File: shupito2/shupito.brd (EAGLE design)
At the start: 41.9 x 26 mm, 84 parts, among them IC2 74LVC1T45, IC3 74LVC1T45, IC4 74LVC1T45, IC5 74LVC1T45, IC6 ATXMEGA32A4U-AU, IC7 TPS73033DBV, Q1 BC807W-1907646, Q10 1758094, Q11 PDTC123YU-1757992, Q2 NX2301P-1894738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

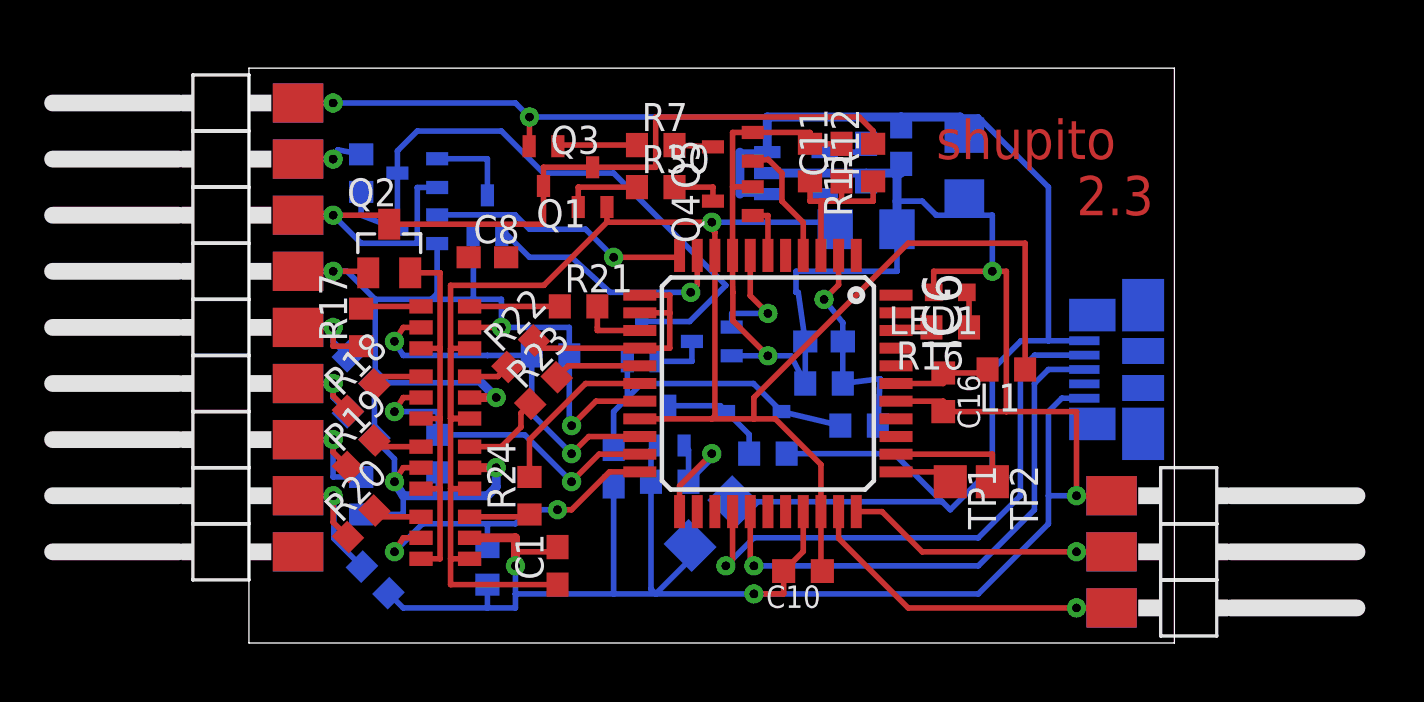
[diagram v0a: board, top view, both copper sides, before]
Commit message: Added a button, placement and routing.
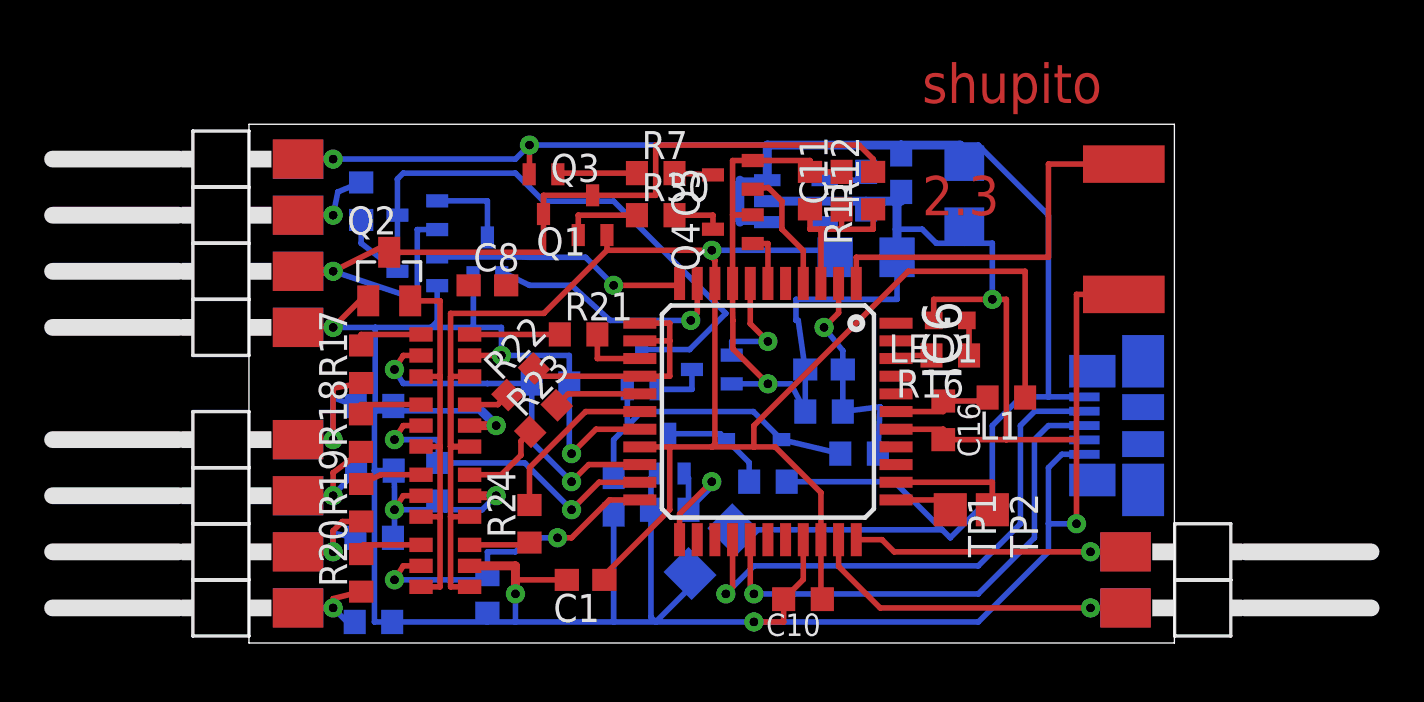
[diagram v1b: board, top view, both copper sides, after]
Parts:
- removed JP19, JP20, JP25, JP27: PINH1X01SMD, pinhead_smd:PINH1X01SMD
- added S1: KSS241G, switch:KSS-G
- moved JP1 5.08 mm to (0.00, 9.53)
- moved JP12 5.08 mm to (0.00, 9.53)
- moved JP15 5.08 mm to (0.00, 4.45)
- moved JP16 5.08 mm to (0.00, 1.91)
- moved JP3 5.08 mm to (0.00, 4.45)
- moved JP4 5.08 mm to (0.00, 1.91)
- moved JP14 5.08 mm to (0.00, 6.99)
- moved JP2 5.08 mm to (0.00, 6.99)
- moved JP23 2.54 mm to (0.00, 19.7)
- moved JP24 2.54 mm to (0.00, 19.7)
- moved JP11 2.54 mm to (0.00, 22.2)
- moved JP13 2.54 mm to (0.00, 17.1)
- moved JP17 2.54 mm to (0.00, 14.6)
- moved JP18 2.54 mm to (0.00, 22.2)
- moved JP5 2.54 mm to (0.00, 17.1)
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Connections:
- new net BTN: IC6.1, S1.2
- net GND: now also S1.1; no longer JP19.1, JP20.1
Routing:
- net BTN: track 0.00 -> 17.5 mm
- net GND: track 205.0 -> 213.4 mm
- net N$37: track 9.09 -> 6.14 mm
- net N$35: track 6.88 -> 9.79 mm
- net D-: track 26.1 -> 24.8 mm
- net D+: track 24.5 -> 23.2 mm
- net VCC: track 92.5 -> 93.7 mm
- net N$7: track 6.27 -> 7.33 mm
- net N$9: track 2.25 -> 3.16 mm
- net N$27: track 2.23 -> 3.04 mm
- net N$8: track 4.72 -> 5.39 mm
- net VCCIO: track 41.5 -> 42.1 mm
- net N$25: track 2.23 -> 2.80 mm
- net N$36: track 7.97 -> 7.45 mm
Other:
- board size 41.9 x 26 mm -> 41.9 x 23.5 mm

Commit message: Routed.
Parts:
- added JP19, JP20: PINH1X01SMD, pinhead_smd:PINH1X01SMD
- added R3, R4: 0, rcl:R1206
- added TP3, TP4, TP5: TPTP15SQ, testpad:TP15SQ
- C1, C11, C4, C5, C8: device rcl:C0603 -> rcl:C0603K
- C13: value 4.7u -> 1u/25V-1759039; device rcl:C0603 -> rcl:C0603K
- C2: value 100n -> 10n; device rcl:C0603 -> rcl:C0603K
- C3: value 4.7u -> 2.2u-1759473; device rcl:C1206 -> rcl:C0603K
- C6: device rcl:C1206 -> rcl:C0603K
- C7: value 4.7u -> 2.2u; device rcl:C1206 -> rcl:C0603K
- L2: value (none) -> 10uH-1463501; device rcl:R0603 -> rcl:R0805
- Q6, Q9: value (none) -> DTA144-1680214
- R11: value 1k5 -> 1k5 1%
- R12, R30, R7: value 6k8 -> 6k8 1%
- R13: value 4k7 -> 15k 1%
- R14: value 4k7 -> 1k 1%
- moved LED1 6.55 mm to (36.8, 19.1), turned to 180 degrees
- moved C4 5.90 mm to (29.7, 15.2), turned to 0 degrees
- moved Q9 5.12 mm to (18.4, 17.8)
- moved IC7 4.84 mm to (29.2, 18.4), turned to 180 degrees
- moved C7 3.22 mm to (35.6, 20.1)
- moved C5 2.89 mm to (32.0, 20.1)
- moved L1 2.84 mm to (33.0, 14.0), turned to 270 degrees
- moved Q1 2.62 mm to (10.8, 20.0)
- moved R16 2.62 mm to (31.1, 15.9), turned to 270 degrees
- moved Q3 2.62 mm to (13.0, 19.1)
- moved D2 2.54 mm to (20.3, 9.53), turned to 270 degrees
- moved C2 2.29 mm to (27.9, 11.4), turned to 270 degrees
- moved Q7 2.22 mm to (21.0, 14.9), turned to 0 degrees
- moved TP1 2.01 mm to (32.4, 4.45)
- moved TP2 2.01 mm to (34.3, 4.45)
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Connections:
- new net GND2: C13.2, C3.2, Q10.2, R2.2, R3.2
- new net N$11: Q9.2, R4.2
- net GND: now also JP19.1, JP20.1, R3.1; no longer C13.2, C3.2, Q10.2, R2.2
- net HIV_ADC: now also IC6.41; no longer IC6.2
- net HIV_LO: now also IC6.10; no longer IC6.11
- net HIV_VCCIO: now also IC6.14; no longer IC6.10
- net LED: now also IC6.43; no longer IC6.42
- net N$22: now also R4.1, TP3.TP; no longer Q9.2
- net RST: now also IC6.11; no longer IC6.14
- net VCC: now also TP4.TP, TP5.TP
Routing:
- net GND2: track 0.00 -> 34.0 mm
- net GND: track 213.4 -> 187.5 mm
- net N$40: track 29.4 -> 19.9 mm
- net N$15: track 1.69 -> 10.4 mm
- net N$29: track 17.7 -> 21.2 mm
- net HIV_VCCIO: track 11.3 -> 8.03 mm
- net N$19: track 3.63 -> 6.81 mm
- net N$11: track 0.00 -> 2.71 mm
- net D+: track 23.2 -> 20.6 mm, vias 1 -> 2
- net N$28: track 3.87 -> 6.41 mm
- net HIV_LO: track 11.5 -> 13.9 mm
- net D-: track 24.8 -> 22.6 mm, vias 1 -> 2
- net RST: track 3.01 -> 5.01 mm
- net N$1: track 14.0 -> 15.9 mm
- net N$3: track 2.90 -> 4.81 mm
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- added copper zone on layer 1, net GND
- added copper zone on layer 16, net GND
- added copper zone on layer 1, net VCC

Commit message: Done.
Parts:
- L2: value 10uH-1463501 -> 10uH-1463501, 22uH-1612131
- R13: value 15k 1% -> 22k 1%
- R14: value 1k 1% -> 1k5 1%
- R2: value 4k7 -> 6k8
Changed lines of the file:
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@@
 <element name="Q7" library="transistors" package="SOT323" value="PDTC123YU-1757992" x="20.955" y="14.9225" rot="MR0"/>
 <element name="Q8" library="transistors" package="SOT323" value="PDTC123YU-1757992" x="7.62" y="17.145" rot="MR270"/>
-<element name="L2" library="rcl" package="R0805" value="10uH-1463501" x="21.9075" y="6.985" rot="MR90"/>
+<element name="L2" library="rcl" package="R0805" value="10uH-1463501, 22uH-1612131" x="21.9075" y="6.985" rot="MR90"/>
 <element name="C13" library="rcl" package="C0603K" value="1u/25V-1759039" x="16.51" y="8.89" rot="MR270"/>
 <element name="D2" library="diode" package="SOD323" value="BAT42WS-1621831" x="20.32" y="9.525" rot="MR270"/>
 <element name="Q10" library="transistors" package="SOT323" value="1758094" x="18.415" y="8.89" rot="MR0"/>
 <element name="R1" library="rcl" package="R0603" value="330" x="5.08" y="19.05" rot="MR270"/>
-<element name="R2" library="rcl" package="R0603" value="4k7" x="18.415" y="6.35" rot="MR0"/>
+<element name="R2" library="rcl" package="R0603" value="6k8" x="18.415" y="6.35" rot="MR0"/>
 <element name="Q9" library="transistors" package="SOT323" value="DTA144-1680214" x="18.415" y="17.78" rot="MR0"/>
-<element name="R13" library="rcl" package="R0603" value="15k 1%" x="26.9875" y="8.89" rot="MR0"/>
-<element name="R14" library="rcl" package="R0603" value="1k 1%" x="26.035" y="11.43" rot="MR270"/>
+<element name="R13" library="rcl" package="R0603" value="22k 1%" x="26.9875" y="8.89" rot="MR0"/>
+<element name="R14" library="rcl" package="R0603" value="1k5 1%" x="26.035" y="11.43" rot="MR270"/>
 <element name="IC6" library="xmega" package="TQFP44" value="ATXMEGA32A4U-AU" x="23.495" y="10.795" rot="R270"/>
 <element name="X2" library="usb" package="USB-MICRO-B-BOTTOM-MOLEX" value="USB-MICRO-B-BOTTOM" x="40.48125" y="10.16" rot="R180"/>

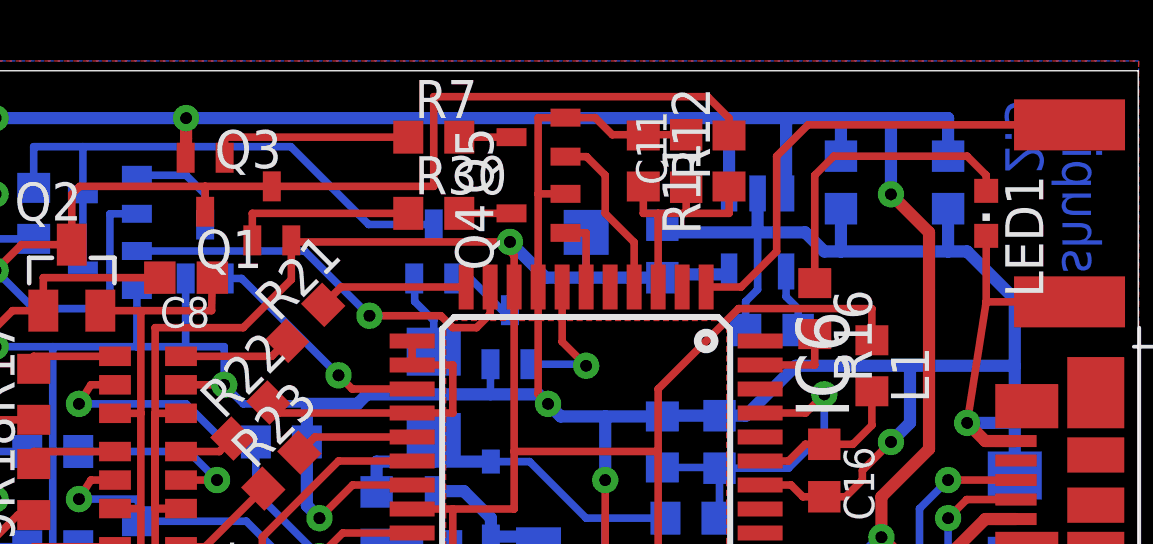
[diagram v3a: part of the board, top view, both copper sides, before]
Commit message: Added a protection diode for the 3.3v ldo.
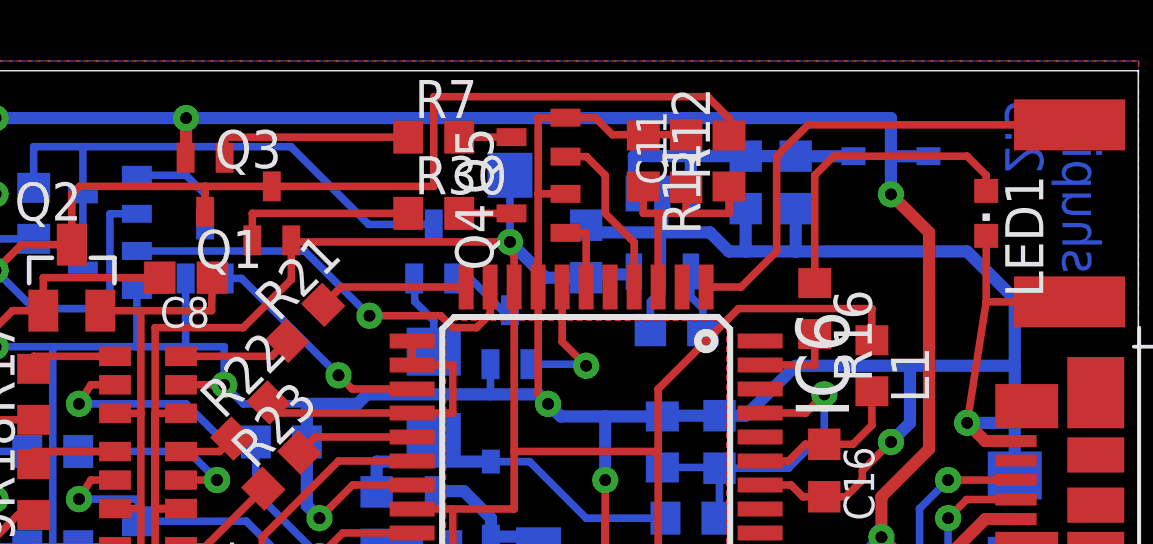
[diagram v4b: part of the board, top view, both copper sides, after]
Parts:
- added D1: BAT42WS-1621831, diode:SOD323
- moved C7 5.08 mm to (30.5, 20.1)
- moved TP4 3.18 mm to (21.0, 20.3)
- moved C4 3.18 mm to (26.5, 15.2)
- moved C5 3.18 mm to (28.8, 20.1)
- moved IC7 3.18 mm to (26.0, 18.4)
- moved C6 2.54 mm to (23.5, 17.8)
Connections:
- new net N$13: C5.1, C7.1, D1.C, IC7.1, IC7.3
- net +5V: now also D1.A; no longer C5.1, C7.1, IC7.1, IC7.3
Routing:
- net N$13: track 0.00 -> 9.81 mm
- net +5V: track 82.1 -> 73.9 mm
- net GND: track 187.5 -> 190.0 mm
- net VCC: track 93.8 -> 91.4 mm

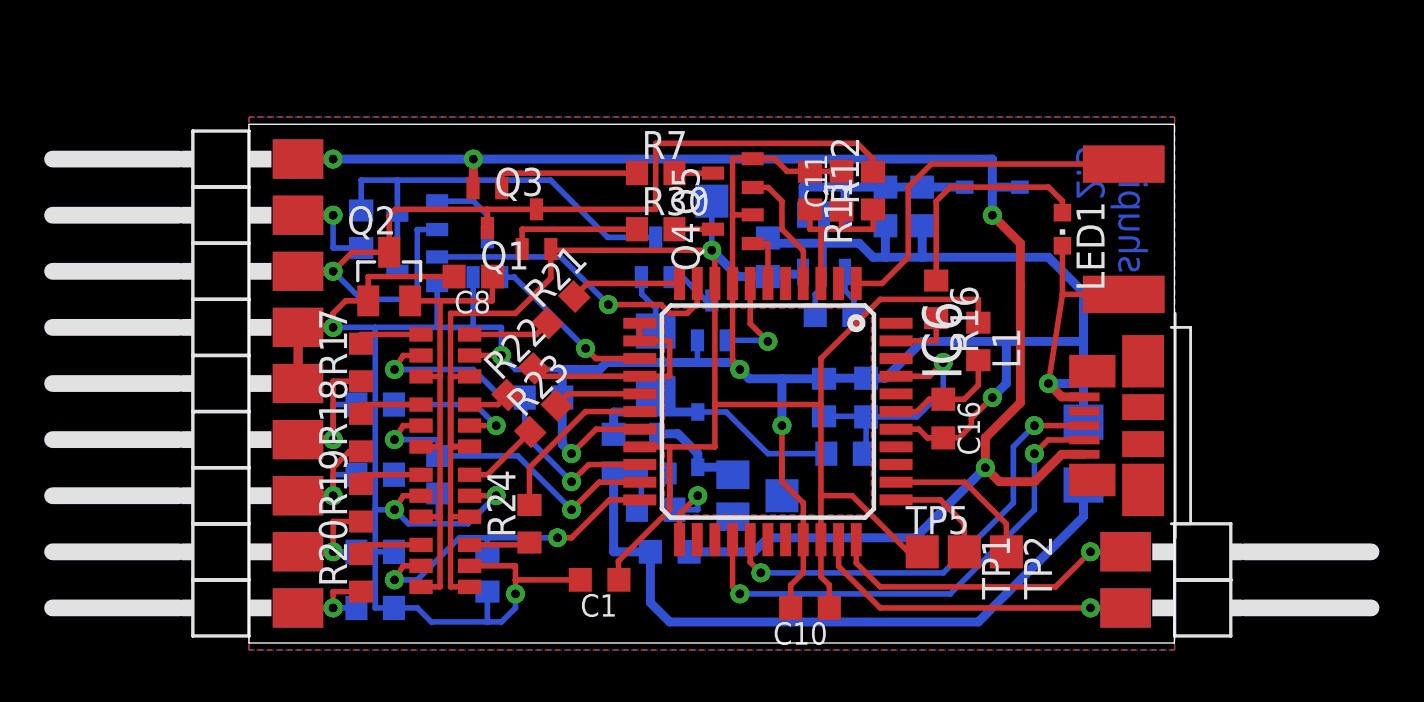
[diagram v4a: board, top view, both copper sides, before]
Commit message: Added GND and VCC to AUX connector.
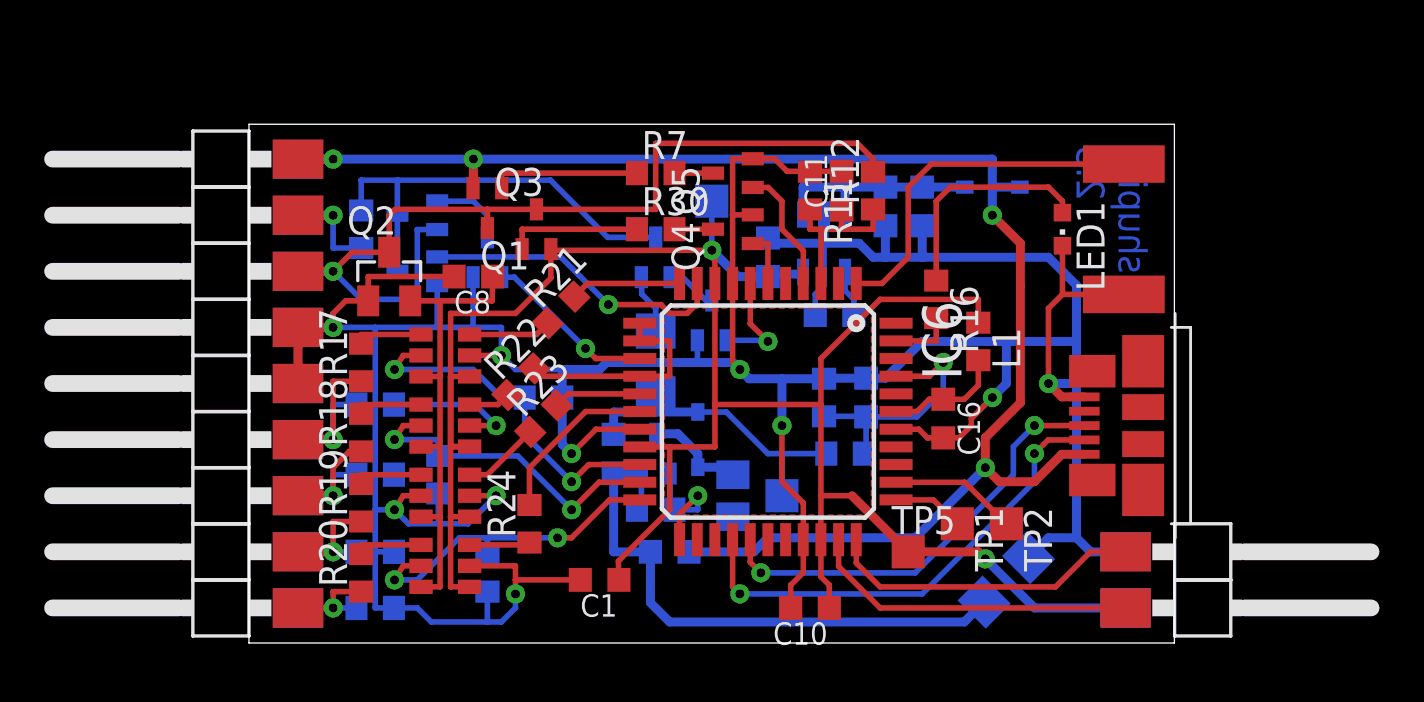
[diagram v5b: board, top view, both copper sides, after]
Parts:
- moved R3 6.70 mm to (34.3, 3.17), turned to 315 degrees
- moved TP1 1.31 mm to (32.1, 5.71)
- moved TP2 1.27 mm to (34.3, 5.71)
- moved TP5 0.64 mm to (29.8, 4.45)
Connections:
- net GND: now also JP8.1
- net N$1: no longer JP8.1
- net N$12: no longer JP10.1
- net VCC: now also JP10.1
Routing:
- net VCC: track 91.4 -> 101.6 mm, vias 1 -> 2
- net GND: track 190.0 -> 199.7 mm
- net GND2: track 34.0 -> 26.5 mm
- net N$1: track 15.9 -> 14.4 mm, vias 1 -> 0
- net N$12: track 16.6 -> 15.0 mm, vias 1 -> 0
- net N$3: track 4.81 -> 3.22 mm
- net N$2: track 7.04 -> 5.77 mm
- net D-: track 22.6 -> 21.8 mm
- net D+: track 20.6 -> 19.9 mm
- removed copper zone on layer 1, net GND
- removed copper zone on layer 16, net GND

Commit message: Added protective resistors.
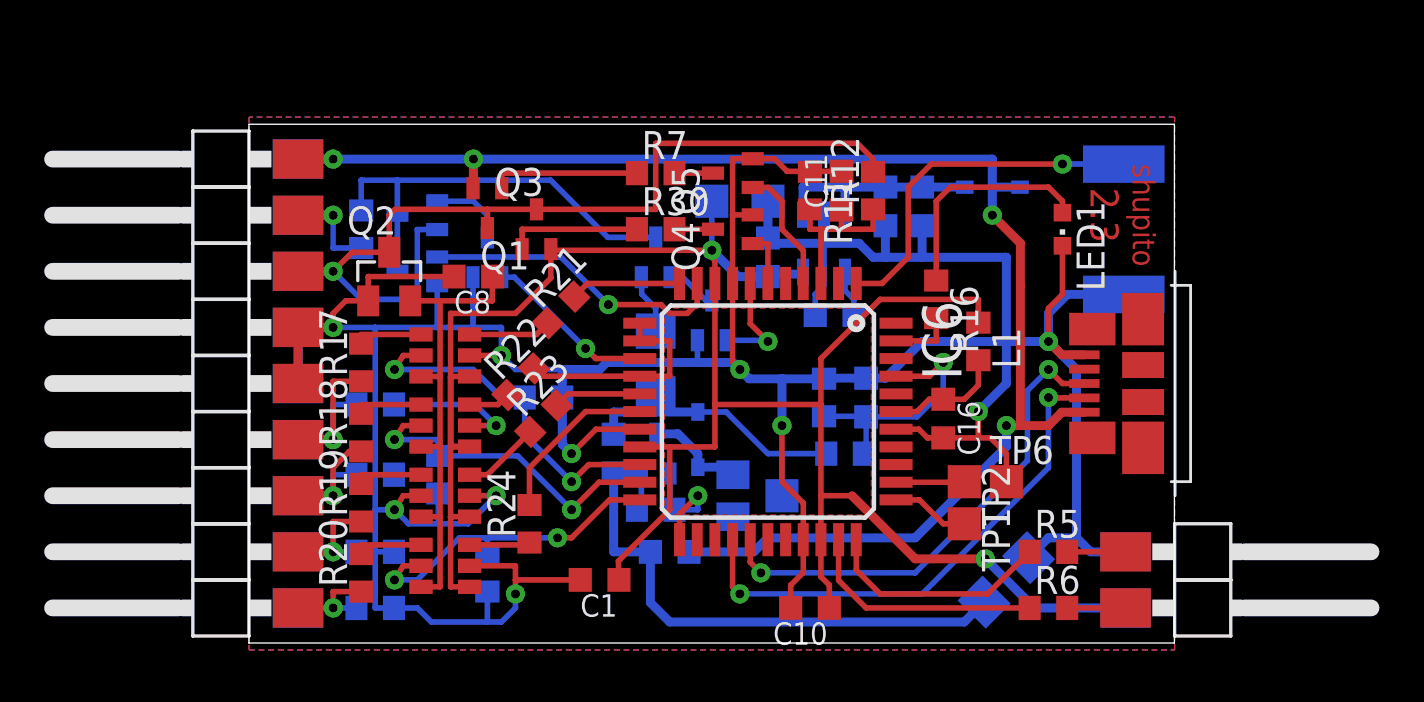
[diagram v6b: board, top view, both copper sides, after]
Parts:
- added R5, R6: 330, rcl:R0603
- added TP6: TPTP15SQ, testpad:TP15SQ
- moved TP5 17.1 mm to (23.5, 20.3), flipped to the bottom
- moved TP2 2.69 mm to (32.4, 7.62)
- moved X2 1.90 mm to (40.5, 12.1)
- moved TP1 0.32 mm to (32.4, 5.71)
- flipped S1 to the bottom
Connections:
- new net N$14: JP7.1, R5.2
- new net N$18: JP9.1, R6.2
- net GND: now also TP5.TP, TP6.TP
- net N$1: now also R5.1; no longer JP7.1
- net N$12: now also R6.1; no longer JP9.1
- net VCC: no longer TP5.TP
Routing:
- net N$12: track 15.0 -> 11.0 mm
- net N$1: track 14.4 -> 10.5 mm
- net N$18: track 0.00 -> 2.64 mm
- net N$14: track 0.00 -> 2.64 mm
- net N$2: track 5.77 -> 3.15 mm
- net D+: track 19.9 -> 22.3 mm
- net D-: track 21.8 -> 23.8 mm
- net +5V: track 73.9 -> 72.1 mm
- net GND: track 199.7 -> 200.7 mm
- net BTN: vias 0 -> 1
- added copper zone on layer 1, net GND
- added copper zone on layer 16, net GND
